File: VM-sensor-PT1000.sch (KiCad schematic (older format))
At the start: 17 parts, among them P1 PT100, P2 ADC, P3 PWR, U1 AMS1117, U2 MCP6001

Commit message: add led PWR & change header ADC
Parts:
- removed P2: ADC, Pin_Headers:Pin_Header_Straight_1x01, symbol CONN_01X01
- added D1: LED, symbol LED
- added P2: ADC, symbol CONN_01X02
- added R9: 10k, Resistors_SMD:R_0805, symbol R_Small
- C3: value lib:C_0603 -> 10uF
- R2: value 100/1% -> 100R/1%
- R3, R6: value 1K/1% -> 16.9K/1%
- R5, R7: value 100K/1% -> 1M/1%
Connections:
- wire segments 43 -> 46
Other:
- moved on the sheet: P3, R5
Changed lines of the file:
@@
 LIBS:valves
 LIBS:AMS1117
+LIBS:VM-sensor-PT1000-cache
 EELAYER 26 0
 EELAYER END
@@
 P 5700 3200
 F 0 "R7" V 5600 3200 50  0000 C CNN
-F 1 "100K/1%" V 5800 3200 50  0000 C CNN
+F 1 "1M/1%" V 5800 3200 50  0000 C CNN
 F 2 "Resistors_SMD:R_0805" H 5700 3200 50  0001 C CNN
 F 3 "" H 5700 3200 50  0000 C CNN
@@
 $EndComp
 $Comp
-L GND #PWR01
+L GND #PWR4
 U 1 1 585E3CDD
 P 6000 3400
-F 0 "#PWR01" H 6000 3150 50  0001 C CNN
+F 0 "#PWR4" H 6000 3150 50  0001 C CNN
 F 1 "GND" H 6000 3250 50  0000 C CNN
 F 2 "" H 6000 3400 50  0000 C CNN
@@
 	1    0    0    -1
 $EndComp
-Text GLabel 8000 3400 1    60   Input ~ 0
+Text GLabel 7750 3650 1    60   Input ~ 0
 VCC
 $Comp
-L GND #PWR02
+L GND #PWR9
 U 1 1 585E400C
 P 7150 3250
-F 0 "#PWR02" H 7150 3000 50  0001 C CNN
+F 0 "#PWR9" H 7150 3000 50  0001 C CNN
 F 1 "GND" H 7150 3100 50  0000 C CNN
 F 2 "" H 7150 3250 50  0000 C CNN
@@
 Blue
 $Comp
-L +3.3V #PWR03
+L +3.3V #PWR2
 U 1 1 585E436C
 P 5200 2250
-F 0 "#PWR03" H 5200 2100 50  0001 C CNN
+F 0 "#PWR2" H 5200 2100 50  0001 C CNN
 F 1 "+3.3V" H 5215 2423 50  0000 C CNN
 F 2 "" H 5200 2250 50  0000 C CNN
@@
 P 4600 3200
 F 0 "R2" H 4659 3246 50  0000 L CNN
-F 1 "100/1%" H 4659 3155 50  0000 L CNN
+F 1 "100R/1%" H 4659 3155 50  0000 L CNN
 F 2 "Resistors_SMD:R_0805" H 4600 3200 50  0001 C CNN
 F 3 "" H 4600 3200 50  0000 C CNN
@@
 P 5050 2950
 F 0 "R3" V 4950 2950 50  0000 C CNN
-F 1 "1K/1%" V 5150 2950 50  0000 C CNN
+F 1 "16.9K/1%" V 5150 2950 50  0000 C CNN
 F 2 "Resistors_SMD:R_0805" H 5050 2950 50  0001 C CNN
 F 3 "" H 5050 2950 50  0000 C CNN
@@
 L R_Small R5
 U 1 1 585E5486
-P 5300 3200
-F 0 "R5" V 5200 3200 50  0000 C CNN
-F 1 "100K/1%" V 5400 3200 50  0000 C CNN
-F 2 "Resistors_SMD:R_0805" H 5300 3200 50  0001 C CNN
-F 3 "" H 5300 3200 50  0000 C CNN
-	1    5300 3200
-	1    0    0    -1
-$EndComp
-$Comp
-L +3.3V #PWR04
+P 5300 3300
+F 0 "R5" V 5200 3300 50  0000 C CNN
+F 1 "1M/1%" V 5400 3300 50  0000 C CNN
+F 2 "Resistors_SMD:R_0805" H 5300 3300 50  0001 C CNN
+F 3 "" H 5300 3300 50  0000 C CNN
+	1    5300 3300
+	1    0    0    -1
+$EndComp
+$Comp
+L +3.3V #PWR3
 U 1 1 585E5570
 P 6000 2500
-F 0 "#PWR04" H 6000 2350 50  0001 C CNN
+F 0 "#PWR3" H 6000 2350 50  0001 C CNN
 F 1 "+3.3V" H 6015 2673 50  0000 C CNN
 F 2 "" H 6000 2500 50  0000 C CNN
@@
 Connection ~ 6600 2850
 Wire Wire Line
-	6000 3400 6000 3150
+	6000 3150 6000 3400
 Wire Wire Line
 	4750 4800 4750 4850
@@
 P 7050 2200
 F 0 "C3" H 7142 2246 50  0000 L CNN
-F 1 "lib:C_0603" H 7142 2155 50  0000 L CNN
+F 1 "10uF" H 7142 2155 50  0000 L CNN
 F 2 "Capacitors_SMD:C_0805" H 7050 2200 50  0001 C CNN
 F 3 "" H 7050 2200 50  0000 C CNN
@@
 $EndComp
 $Comp
-L +3.3V #PWR05
+L +3.3V #PWR6
 U 1 1 585E5A68
 P 7050 2050
-F 0 "#PWR05" H 7050 1900 50  0001 C CNN
+F 0 "#PWR6" H 7050 1900 50  0001 C CNN
 F 1 "+3.3V" H 7065 2223 50  0000 C CNN
 F 2 "" H 7050 2050 50  0000 C CNN
@@
 $EndComp
 $Comp
-L GND #PWR06
+L GND #PWR7
 U 1 1 585E5AC7
 P 7050 2350
-F 0 "#PWR06" H 7050 2100 50  0001 C CNN
+F 0 "#PWR7" H 7050 2100 50  0001 C CNN
 F 1 "GND" H 7050 2200 50  0000 C CNN
 F 2 "" H 7050 2350 50  0000 C CNN
@@
 $EndComp
 $Comp
-L GND #PWR07
+L GND #PWR5
 U 1 1 585E5E26
 P 6100 5500
-F 0 "#PWR07" H 6100 5250 50  0001 C CNN
+F 0 "#PWR5" H 6100 5250 50  0001 C CNN
 F 1 "GND" H 6105 5327 50  0000 C CNN
 F 2 "" H 6100 5500 50  0000 C CNN
@@
 	5200 5150 5200 5450
 Wire Wire Line
-	5200 5450 7050 5450
+	5200 5450 7600 5450
 Connection ~ 6100 5450
 Wire Wire Line
@@
 	7050 4800 7050 5000
 Wire Wire Line
-	7050 4850 6900 4850
-$Comp
-L +3.3V #PWR08
+	6900 4850 7600 4850
+$Comp
+L +3.3V #PWR8
 U 1 1 585E60F4
 P 7050 4800
-F 0 "#PWR08" H 7050 4650 50  0001 C CNN
+F 0 "#PWR8" H 7050 4650 50  0001 C CNN
 F 1 "+3.3V" H 7065 4973 50  0000 C CNN
 F 2 "" H 7050 4800 50  0000 C CNN
@@
 P 5500 2750
 F 0 "R6" V 5400 2750 50  0000 C CNN
-F 1 "1K/1%" V 5600 2750 50  0000 C CNN
+F 1 "16.9K/1%" V 5600 2750 50  0000 C CNN
 F 2 "Resistors_SMD:R_0805" H 5500 2750 50  0001 C CNN
 F 3 "" H 5500 2750 50  0000 C CNN
@@
 	5150 2950 5800 2950
 Wire Wire Line
-	5300 2950 5300 3100
+	5300 2950 5300 3200
 Connection ~ 5300 2950
 Wire Wire Line
-	5300 3300 5300 3650
+	5300 3400 5300 3650
 Wire Wire Line
 	5300 3650 6600 3650
@@
 Connection ~ 4600 2950
 $Comp
-L GND #PWR09
+L GND #PWR1
 U 1 1 585E7E19
 P 4600 3400
-F 0 "#PWR09" H 4600 3150 50  0001 C CNN
+F 0 "#PWR1" H 4600 3150 50  0001 C CNN
 F 1 "GND" H 4600 3250 50  0000 C CNN
 F 2 "" H 4600 3400 50  0000 C CNN
@@
 L CONN_01X02 P3
 U 1 1 58609B23
-P 8250 3500
-F 0 "P3" H 8328 3541 50  0000 L CNN
-F 1 "PWR" H 8328 3450 50  0000 L CNN
-F 2 "Pin_Headers:Pin_Header_Straight_1x02" H 8250 3500 50  0001 C CNN
-F 3 "" H 8250 3500 50  0000 C CNN
-	1    8250 3500
-	1    0    0    -1
-$EndComp
-$Comp
-L CONN_01X01 P2
-U 1 1 58609B7F
-P 8000 2850
-F 0 "P2" H 8078 2891 50  0000 L CNN
-F 1 "ADC" H 8078 2800 50  0000 L CNN
-F 2 "Pin_Headers:Pin_Header_Straight_1x01" H 8000 2850 50  0001 C CNN
-F 3 "" H 8000 2850 50  0000 C CNN
-	1    8000 2850
-	1    0    0    -1
-$EndComp
-Wire Wire Line
-	8000 3400 8000 3450
-Wire Wire Line
-	8000 3450 8050 3450
-$Comp
-L GND #PWR010
+P 8000 3750
+F 0 "P3" H 8078 3791 50  0000 L CNN
+F 1 "PWR" H 8078 3700 50  0000 L CNN
+F 2 "Pin_Headers:Pin_Header_Straight_1x02" H 8000 3750 50  0001 C CNN
+F 3 "" H 8000 3750 50  0000 C CNN
+	1    8000 3750
+	1    0    0    -1
+$EndComp
+Wire Wire Line
+	7750 3650 7750 3700
+Wire Wire Line
+	7750 3700 7800 3700
+$Comp
+L GND #PWR10
 U 1 1 5860A0C0
-P 8000 3600
-F 0 "#PWR010" H 8000 3350 50  0001 C CNN
-F 1 "GND" H 8005 3427 50  0000 C CNN
-F 2 "" H 8000 3600 50  0000 C CNN
-F 3 "" H 8000 3600 50  0000 C CNN
-	1    8000 3600
-	1    0    0    -1
-$EndComp
-Wire Wire Line
-	8050 3550 8000 3550
-Wire Wire Line
-	8000 3550 8000 3600
+P 7750 3850
+F 0 "#PWR10" H 7750 3600 50  0001 C CNN
+F 1 "GND" H 7755 3677 50  0000 C CNN
+F 2 "" H 7750 3850 50  0000 C CNN
+F 3 "" H 7750 3850 50  0000 C CNN
+	1    7750 3850
+	1    0    0    -1
+$EndComp
+Wire Wire Line
+	7800 3800 7750 3800
+Wire Wire Line
+	7750 3800 7750 3850
+$Comp
+L CONN_01X02 P2
+U 1 1 586F4E69
+P 8000 2900
+F 0 "P2" H 8078 2941 50  0000 L CNN
+F 1 "ADC" H 8078 2850 50  0000 L CNN
+F 2 "" H 8000 2900 50  0000 C CNN
+F 3 "" H 8000 2900 50  0000 C CNN
+	1    8000 2900
+	1    0    0    -1
+$EndComp
+$Comp
+L GND #PWR11
+U 1 1 586F4F66
+P 7800 3050
+F 0 "#PWR11" H 7800 2800 50  0001 C CNN
+F 1 "GND" H 7805 2877 50  0000 C CNN
+F 2 "" H 7800 3050 50  0000 C CNN
+F 3 "" H 7800 3050 50  0000 C CNN
+	1    7800 3050
+	1    0    0    -1
+$EndComp
+Wire Wire Line
+	7800 2950 7800 3050
+$Comp
+L LED D1
+U 1 1 586F5115
+P 7600 5250
+F 0 "D1" V 7638 5133 50  0000 R CNN
+F 1 "LED" V 7547 5133 50  0000 R CNN
+F 2 "" H 7600 5250 50  0000 C CNN
+F 3 "" H 7600 5250 50  0000 C CNN
+	1    7600 5250
+	0    -1   -1   0
+$EndComp
+Wire Wire Line
+	7600 5450 7600 5400
+Connection ~ 7050 5450
+$Comp
+L R_Small R9
+U 1 1 586F5264
+P 7600 4950
+F 0 "R9" H 7659 4996 50  0000 L CNN
+F 1 "10k" H 7659 4905 50  0000 L CNN
+F 2 "Resistors_SMD:R_0805" H 7600 4950 50  0001 C CNN
+F 3 "" H 7600 4950 50  0000 C CNN
+	1    7600 4950
+	1    0    0    -1
+$EndComp
+Wire Wire Line
+	7600 5050 7600 5100
 $EndSCHEMATC

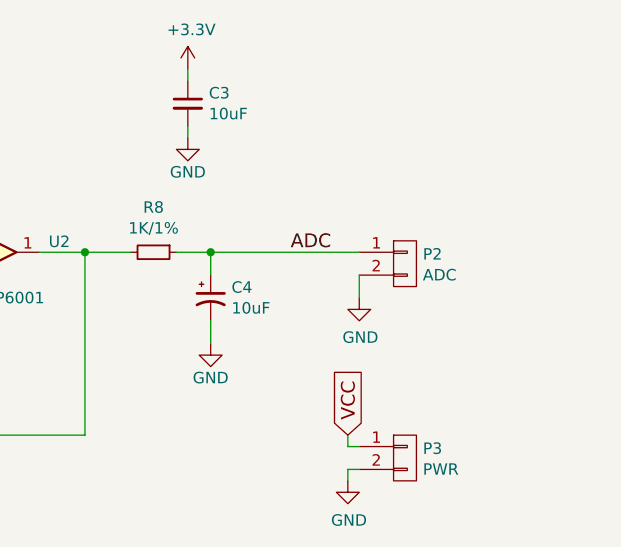
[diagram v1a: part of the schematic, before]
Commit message: add led PWR & change header ADC
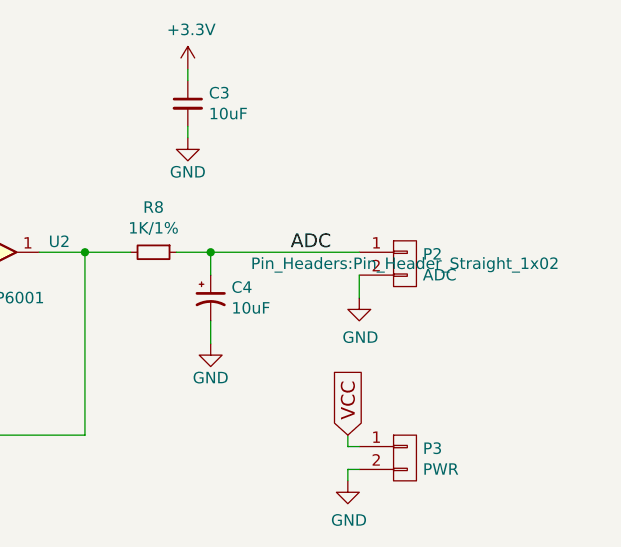
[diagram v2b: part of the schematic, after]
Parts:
- P2: footprint (none) -> Pin_Headers:Pin_Header_Straight_1x02
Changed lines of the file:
@@
 F 0 "P2" H 8078 2941 50  0000 L CNN
 F 1 "ADC" H 8078 2850 50  0000 L CNN
-F 2 "" H 8000 2900 50  0000 C CNN
+F 2 "Pin_Headers:Pin_Header_Straight_1x02" H 8000 2900 50  0000 C CNN
 F 3 "" H 8000 2900 50  0000 C CNN
 	1    8000 2900

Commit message: completed new PCB design
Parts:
- removed D1: LED, symbol LED
- removed P1: PT100, Connectors_Hirose:Hirose_DF63-3P-3.96DSA_03x3.96mm_Straight, symbol CONN_01X03
- added D1: LED_Small, LEDs:LED-3MM, symbol LED_Small
- added P1: PT100, lib:Domino-PT100.pretty, symbol CONN_01X04
- P2, P3: footprint Pin_Headers:Pin_Header_Straight_1x02 -> w_conn_jst-ph:s2b-ph-kl
- R9: value 10k -> 100R/1%
- U2: value MCP6001 -> MCP601T
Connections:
- wire segments 46 -> 47
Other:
- moved on the sheet: P3, R2, R5
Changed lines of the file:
@@
 P 6100 2850
 F 0 "U2" H 6441 2896 50  0000 L CNN
-F 1 "MCP6001" H 6100 2650 50  0000 L CNN
+F 1 "MCP601T" H 6100 2650 50  0000 L CNN
 F 2 "TO_SOT_Packages_SMD:SOT-23-5" H 6050 2950 50  0001 C CNN
 F 3 "" H 6150 3050 50  0000 C CNN
@@
 	1    6100 4850
 	1    0    0    -1
-$EndComp
-$Comp
-L CONN_01X03 P1
-U 1 1 585E368F
-P 3650 2850
-F 0 "P1" H 3650 2650 50  0000 C CNN
-F 1 "PT100" H 3650 3100 50  0000 C CNN
-F 2 "Connectors_Hirose:Hirose_DF63-3P-3.96DSA_03x3.96mm_Straight" H 3650 2850 50  0001 C CNN
-F 3 "" H 3650 2850 50  0000 C CNN
-	1    3650 2850
-	-1   0    0    1
 $EndComp
 $Comp
@@
 $EndComp
 $Comp
-L GND #PWR4
+L GND #PWR01
 U 1 1 585E3CDD
 P 6000 3400
-F 0 "#PWR4" H 6000 3150 50  0001 C CNN
+F 0 "#PWR01" H 6000 3150 50  0001 C CNN
 F 1 "GND" H 6000 3250 50  0000 C CNN
 F 2 "" H 6000 3400 50  0000 C CNN
@@
 	1    0    0    -1
 $EndComp
-Text GLabel 7750 3650 1    60   Input ~ 0
+Text GLabel 8000 3700 1    60   Input ~ 0
 VCC
 $Comp
-L GND #PWR9
+L GND #PWR02
 U 1 1 585E400C
 P 7150 3250
-F 0 "#PWR9" H 7150 3000 50  0001 C CNN
+F 0 "#PWR02" H 7150 3000 50  0001 C CNN
 F 1 "GND" H 7150 3100 50  0000 C CNN
 F 2 "" H 7150 3250 50  0000 C CNN
@@
 Blue
 $Comp
-L +3.3V #PWR2
+L +3.3V #PWR03
 U 1 1 585E436C
 P 5200 2250
-F 0 "#PWR2" H 5200 2100 50  0001 C CNN
+F 0 "#PWR03" H 5200 2100 50  0001 C CNN
 F 1 "+3.3V" H 5215 2423 50  0000 C CNN
 F 2 "" H 5200 2250 50  0000 C CNN
@@
 L R_Small R2
 U 1 1 585E512A
-P 4600 3200
-F 0 "R2" H 4659 3246 50  0000 L CNN
-F 1 "100R/1%" H 4659 3155 50  0000 L CNN
-F 2 "Resistors_SMD:R_0805" H 4600 3200 50  0001 C CNN
-F 3 "" H 4600 3200 50  0000 C CNN
-	1    4600 3200
+P 4600 3150
+F 0 "R2" H 4659 3196 50  0000 L CNN
+F 1 "100R/1%" H 4659 3105 50  0000 L CNN
+F 2 "Resistors_SMD:R_0805" H 4600 3150 50  0001 C CNN
+F 3 "" H 4600 3150 50  0000 C CNN
+	1    4600 3150
 	1    0    0    -1
 $EndComp
@@
 L R_Small R5
 U 1 1 585E5486
-P 5300 3300
-F 0 "R5" V 5200 3300 50  0000 C CNN
-F 1 "1M/1%" V 5400 3300 50  0000 C CNN
-F 2 "Resistors_SMD:R_0805" H 5300 3300 50  0001 C CNN
-F 3 "" H 5300 3300 50  0000 C CNN
-	1    5300 3300
-	1    0    0    -1
-$EndComp
-$Comp
-L +3.3V #PWR3
+P 5300 3200
+F 0 "R5" V 5200 3200 50  0000 C CNN
+F 1 "1M/1%" V 5400 3200 50  0000 C CNN
+F 2 "Resistors_SMD:R_0805" H 5300 3200 50  0001 C CNN
+F 3 "" H 5300 3200 50  0000 C CNN
+	1    5300 3200
+	1    0    0    -1
+$EndComp
+$Comp
+L +3.3V #PWR04
 U 1 1 585E5570
 P 6000 2500
-F 0 "#PWR3" H 6000 2350 50  0001 C CNN
+F 0 "#PWR04" H 6000 2350 50  0001 C CNN
 F 1 "+3.3V" H 6015 2673 50  0000 C CNN
 F 2 "" H 6000 2500 50  0000 C CNN
@@
 $EndComp
 $Comp
-L +3.3V #PWR6
+L +3.3V #PWR05
 U 1 1 585E5A68
 P 7050 2050
-F 0 "#PWR6" H 7050 1900 50  0001 C CNN
+F 0 "#PWR05" H 7050 1900 50  0001 C CNN
 F 1 "+3.3V" H 7065 2223 50  0000 C CNN
 F 2 "" H 7050 2050 50  0000 C CNN
@@
 $EndComp
 $Comp
-L GND #PWR7
+L GND #PWR06
 U 1 1 585E5AC7
 P 7050 2350
-F 0 "#PWR7" H 7050 2100 50  0001 C CNN
+F 0 "#PWR06" H 7050 2100 50  0001 C CNN
 F 1 "GND" H 7050 2200 50  0000 C CNN
 F 2 "" H 7050 2350 50  0000 C CNN
@@
 $EndComp
 $Comp
-L GND #PWR5
+L GND #PWR07
 U 1 1 585E5E26
 P 6100 5500
-F 0 "#PWR5" H 6100 5250 50  0001 C CNN
+F 0 "#PWR07" H 6100 5250 50  0001 C CNN
 F 1 "GND" H 6105 5327 50  0000 C CNN
 F 2 "" H 6100 5500 50  0000 C CNN
@@
 	6900 4850 7600 4850
 $Comp
-L +3.3V #PWR8
+L +3.3V #PWR08
 U 1 1 585E60F4
 P 7050 4800
-F 0 "#PWR8" H 7050 4650 50  0001 C CNN
+F 0 "#PWR08" H 7050 4650 50  0001 C CNN
 F 1 "+3.3V" H 7065 4973 50  0000 C CNN
 F 2 "" H 7050 4800 50  0000 C CNN
@@
 	5150 2950 5800 2950
 Wire Wire Line
-	5300 2950 5300 3200
+	5300 2950 5300 3100
 Connection ~ 5300 2950
 Wire Wire Line
-	5300 3400 5300 3650
+	5300 3300 5300 3650
 Wire Wire Line
 	5300 3650 6600 3650
@@
 Connection ~ 6000 3350
 Wire Wire Line
-	4600 2550 4600 3100
+	4600 2550 4600 3050
 Wire Wire Line
 	4600 2950 4950 2950
 Connection ~ 4600 2950
 $Comp
-L GND #PWR1
+L GND #PWR09
 U 1 1 585E7E19
 P 4600 3400
-F 0 "#PWR1" H 4600 3150 50  0001 C CNN
+F 0 "#PWR09" H 4600 3150 50  0001 C CNN
 F 1 "GND" H 4600 3250 50  0000 C CNN
 F 2 "" H 4600 3400 50  0000 C CNN
@@
 $EndComp
 Wire Wire Line
-	4600 3300 4600 3400
+	4600 3250 4600 3400
 Wire Wire Line
 	4150 2950 4150 3350
@@
 L CONN_01X02 P3
 U 1 1 58609B23
-P 8000 3750
-F 0 "P3" H 8078 3791 50  0000 L CNN
-F 1 "PWR" H 8078 3700 50  0000 L CNN
-F 2 "Pin_Headers:Pin_Header_Straight_1x02" H 8000 3750 50  0001 C CNN
-F 3 "" H 8000 3750 50  0000 C CNN
-	1    8000 3750
-	1    0    0    -1
-$EndComp
-Wire Wire Line
-	7750 3650 7750 3700
-Wire Wire Line
-	7750 3700 7800 3700
-$Comp
-L GND #PWR10
-U 1 1 5860A0C0
-P 7750 3850
-F 0 "#PWR10" H 7750 3600 50  0001 C CNN
-F 1 "GND" H 7755 3677 50  0000 C CNN
-F 2 "" H 7750 3850 50  0000 C CNN
-F 3 "" H 7750 3850 50  0000 C CNN
-	1    7750 3850
-	1    0    0    -1
-$EndComp
-Wire Wire Line
-	7800 3800 7750 3800
-Wire Wire Line
-	7750 3800 7750 3850
+P 8250 3800
+F 0 "P3" H 8328 3841 50  0000 L CNN
+F 1 "PWR" H 8328 3750 50  0000 L CNN
+F 2 "w_conn_jst-ph:s2b-ph-kl" H 8250 3800 50  0001 C CNN
+F 3 "" H 8250 3800 50  0000 C CNN
+	1    8250 3800
+	1    0    0    -1
+$EndComp
+Wire Wire Line
+	8000 3700 8000 3750
+Wire Wire Line
+	8000 3750 8050 3750
+$Comp
+L GND #PWR010
+U 1 1 58705309
+P 8050 3900
+F 0 "#PWR010" H 8050 3650 50  0001 C CNN
+F 1 "GND" H 8055 3727 50  0000 C CNN
+F 2 "" H 8050 3900 50  0000 C CNN
+F 3 "" H 8050 3900 50  0000 C CNN
+	1    8050 3900
+	1    0    0    -1
+$EndComp
+Wire Wire Line
+	8050 3850 8050 3900
+$Comp
+L LED_Small D1
+U 1 1 58705E7D
+P 7600 5250
+F 0 "D1" V 7646 5182 50  0000 R CNN
+F 1 "LED_Small" V 7555 5182 50  0000 R CNN
+F 2 "LEDs:LED-3MM" V 7600 5250 50  0001 C CNN
+F 3 "" V 7600 5250 50  0000 C CNN
+	1    7600 5250
+	0    -1   -1   0
+$EndComp
+$Comp
+L R_Small R9
+U 1 1 58705FCE
+P 7600 5000
+F 0 "R9" H 7500 5000 50  0000 C CNN
+F 1 "100R/1%" H 7400 5100 50  0000 C CNN
+F 2 "Resistors_SMD:R_0805" H 7600 5000 50  0001 C CNN
+F 3 "" H 7600 5000 50  0000 C CNN
+	1    7600 5000
+	-1   0    0    1
+$EndComp
+Wire Wire Line
+	7600 4850 7600 4900
+Wire Wire Line
+	7600 5100 7600 5150
+Wire Wire Line
+	7600 5450 7600 5350
+Connection ~ 7050 5450
 $Comp
 L CONN_01X02 P2
-U 1 1 586F4E69
+U 1 1 58706913
 P 8000 2900
 F 0 "P2" H 8078 2941 50  0000 L CNN
 F 1 "ADC" H 8078 2850 50  0000 L CNN
-F 2 "Pin_Headers:Pin_Header_Straight_1x02" H 8000 2900 50  0000 C CNN
+F 2 "w_conn_jst-ph:s2b-ph-kl" H 8000 2900 50  0001 C CNN
 F 3 "" H 8000 2900 50  0000 C CNN
 	1    8000 2900
@@
 $EndComp
 $Comp
-L GND #PWR11
-U 1 1 586F4F66
-P 7800 3050
-F 0 "#PWR11" H 7800 2800 50  0001 C CNN
-F 1 "GND" H 7805 2877 50  0000 C CNN
-F 2 "" H 7800 3050 50  0000 C CNN
-F 3 "" H 7800 3050 50  0000 C CNN
-	1    7800 3050
-	1    0    0    -1
-$EndComp
-Wire Wire Line
-	7800 2950 7800 3050
-$Comp
-L LED D1
-U 1 1 586F5115
-P 7600 5250
-F 0 "D1" V 7638 5133 50  0000 R CNN
-F 1 "LED" V 7547 5133 50  0000 R CNN
-F 2 "" H 7600 5250 50  0000 C CNN
-F 3 "" H 7600 5250 50  0000 C CNN
-	1    7600 5250
-	0    -1   -1   0
-$EndComp
-Wire Wire Line
-	7600 5450 7600 5400
-Connection ~ 7050 5450
-$Comp
-L R_Small R9
-U 1 1 586F5264
-P 7600 4950
-F 0 "R9" H 7659 4996 50  0000 L CNN
-F 1 "10k" H 7659 4905 50  0000 L CNN
-F 2 "Resistors_SMD:R_0805" H 7600 4950 50  0001 C CNN
-F 3 "" H 7600 4950 50  0000 C CNN
-	1    7600 4950
-	1    0    0    -1
-$EndComp
-Wire Wire Line
-	7600 5050 7600 5100
+L GND #PWR011
+U 1 1 58706988
+P 7800 3000
+F 0 "#PWR011" H 7800 2750 50  0001 C CNN
+F 1 "GND" H 7805 2827 50  0000 C CNN
+F 2 "" H 7800 3000 50  0000 C CNN
+F 3 "" H 7800 3000 50  0000 C CNN
+	1    7800 3000
+	1    0    0    -1
+$EndComp
+Wire Wire Line
+	7800 2950 7800 3000
+$Comp
+L CONN_01X04 P1
+U 1 1 587074AE
+P 3650 2900
+F 0 "P1" H 3569 2525 50  0000 C CNN
+F 1 "PT100" H 3569 2616 50  0000 C CNN
+F 2 "lib:Domino-PT100.pretty" H 3650 2900 50  0001 C CNN
+F 3 "" H 3650 2900 50  0000 C CNN
+	1    3650 2900
+	-1   0    0    1
+$EndComp
+Wire Wire Line
+	3850 3050 4150 3050
+Connection ~ 4150 3050
 $EndSCHEMATC
